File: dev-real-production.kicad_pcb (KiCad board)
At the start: 4 copper layers, 105 x 105 mm, 320 parts, among them IC1 ICM-42670-P, IC2 ENS161-BLGT_LGA9_T&R_1k5, J1 VIN_IN, J10 USB-C USB2 DEBUG, J11 ARM_JTAG_10, J12 SOP0_SELECT, J13 SOP1_SELECT, J14 Conn_01x03, J15 Conn_01x03, J16 ARM_JTAG_10, J17 USB-C Receptacle USB2, J18 Conn_01x03_Pin, J19 Cortex SWD/JTAG, J2 TP_EN_PG, J20 USB-C USB2 DEVICE, J21 HR911105A MAGJACK, J22 Conn_02x10_Counter_Clockwise, J23 Conn_02x04_Odd_Even, J3 TP_SW_FB, J4 USB-C Receptacle USB2, J5 Conn_01x03_Pin, J6 ARM_Cortex_Debug_10, J7 SMA_ANT_50OHM, J8 3V3_IN, U1 MMC5633NJL, U10 USBLC6-2P6, U11 FT230XS-R, U12 FT230XS-R, U13 IWRL6432BDBAAMFR, U14 MX25R1635FZUIH0, U15 MX25R1635FZUIH0, U16 AMS1117-1.8, U17 THS8136, U18 MM8108-MF15457, U19 AP2112K-1.8, U2 LPS22HH, U20 PGA113AIDGSR, U21 AD9609BCPZRL7-80, U22 MCP6D11T-E/MS, U23 STM32H7S3Z8T6, U24 LAN8742A-CZ-TR, U25 USBLC6-2SC6, U3 MIC28516T-E/PHA, U4 RP2350B, U5 XCC1352R1F3RGZR, U6 XMSSJJ3G0PA-054, U7 TLV75518PDBV, U8 TLV75518PDBVR, U9 USBLC6-2P6, Y1 12MHz ABM8-272-T3, Y2 48MHz, Y3 40MHz, Y4 40MHz, Y5 24MHz, Y6 32.768kHz, Y7 25MHz

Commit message: pcb: clean basic DRC findings and document remaining work
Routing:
- net /XCC1352R1F3RGZR/DIO_20: track 135.2 -> 100.4 mm, vias 5 -> 4
- net /XCC1352R1F3RGZR/DIO_26: track 168.3 -> 136.7 mm
- net /STM32H7/PM0: track 102.9 -> 79.9 mm
- net /THX8136/M2: track 176.6 -> 159.4 mm
- net /XCC1352R1F3RGZR/DIO_11: track 138.8 -> 123.2 mm
- net /IWRL6432BD/JTAG_TCK: track 61.8 -> 46.3 mm
- net /RP2350/GPIO7: track 117.0 -> 101.7 mm
- net /STM32H7/PM2: track 85.8 -> 73.0 mm
- net /STM32H7/PM3: track 121.8 -> 114.3 mm
- net /XCC1352R1F3RGZR/DIO_19: track 110.3 -> 103.4 mm
- net /AD9609/RBIAS: track 59.7 -> 53.7 mm
- net /XCC1352R1F3RGZR/DIO_21: track 124.9 -> 119.4 mm
- net /STM32H7/PHY_TXN: track 51.2 -> 45.9 mm
- net /IWRL6432BD/FT_TXD: track 38.1 -> 34.4 mm, vias 6 -> 5
- net /STM32H7/PB5: track 76.0 -> 72.3 mm
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
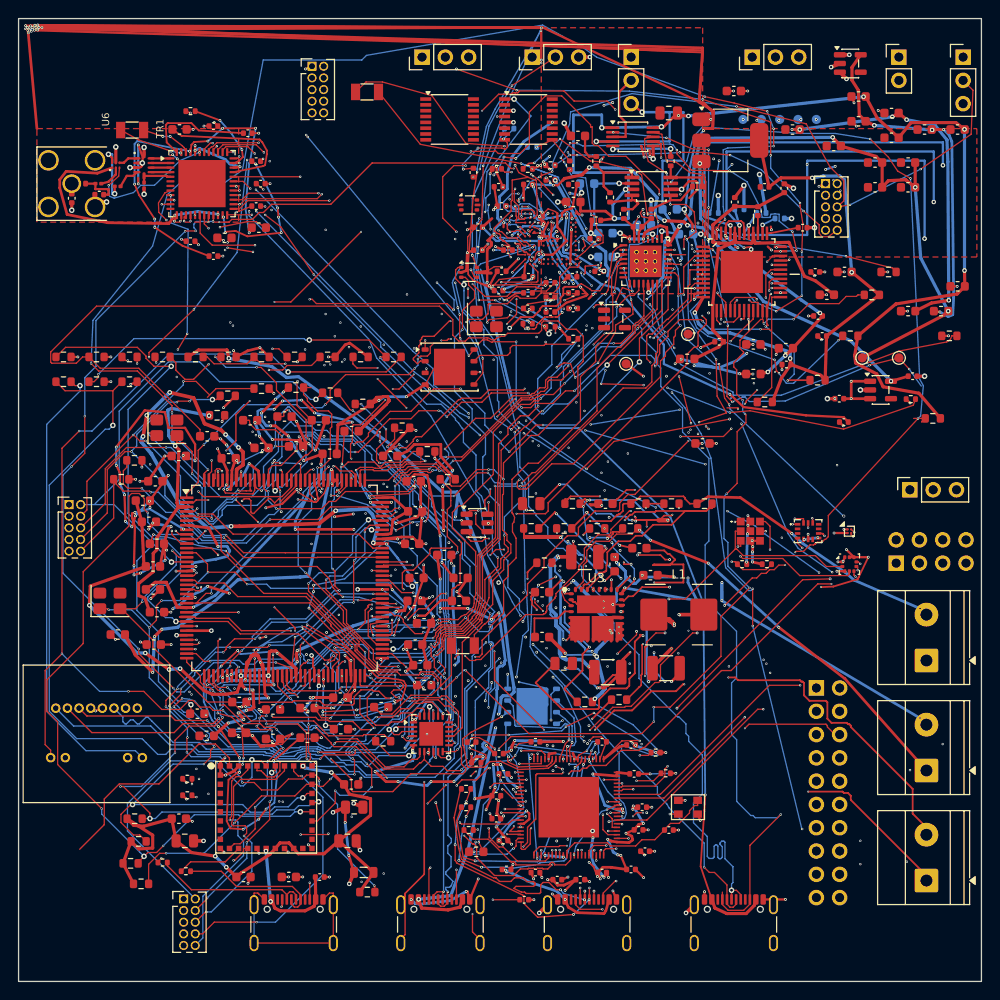
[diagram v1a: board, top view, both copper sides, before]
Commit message: pcb: remove dangling copper and refill zones
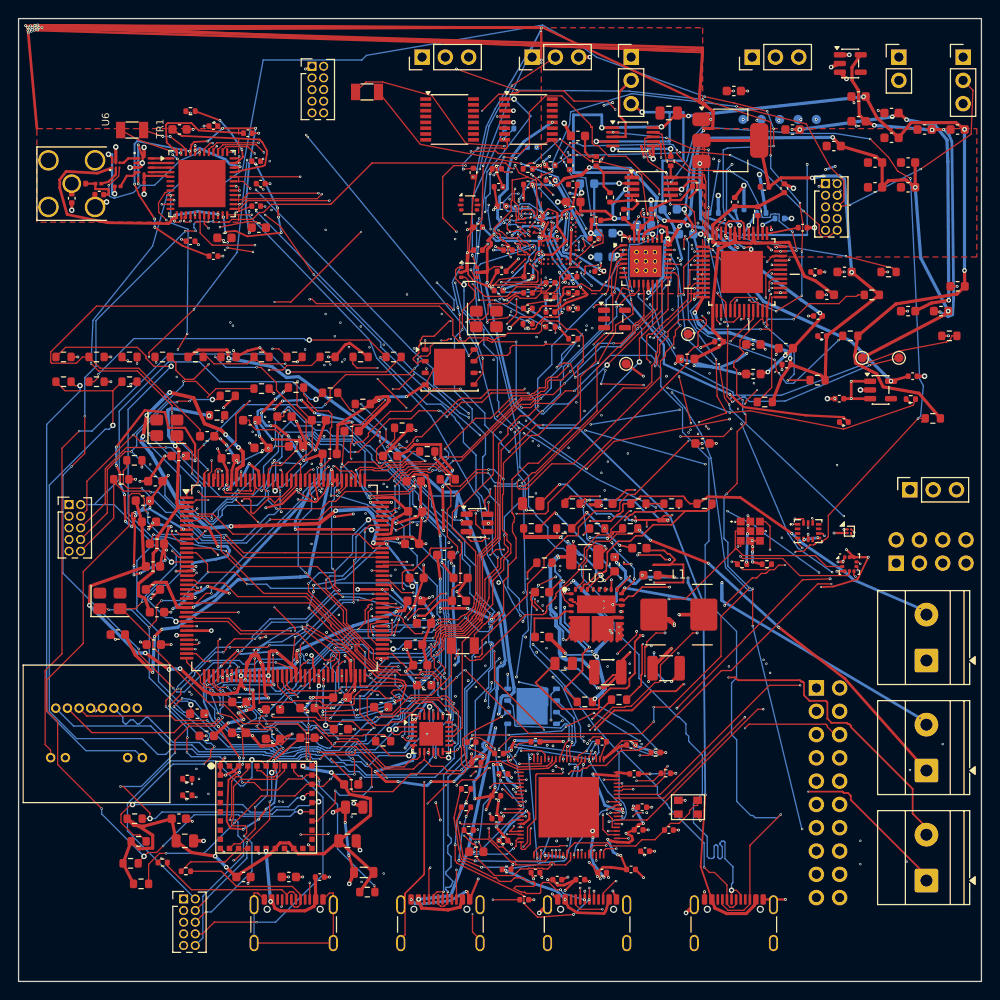
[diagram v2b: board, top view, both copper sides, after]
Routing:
- net /THX8136/AB: track 60.3 -> 23.7 mm, vias 4 -> 3
- net /THX8136/AR: track 51.9 -> 17.3 mm, vias 4 -> 3
- net /THX8136/AG: track 53.1 -> 23.7 mm, vias 4 -> 3
- net /STM32H7/RJ_LED_GREEN_A: track 101.9 -> 77.5 mm, vias 5 -> 2
- net /MM8108/ANT: track 24.2 -> 0.00 mm
- net /IWRL6432BD/GPIO_7: track 109.4 -> 90.5 mm
- net /IWRL6432BD/USB_VBUS: track 136.0 -> 119.8 mm
- net +3V3: track 506.9 -> 496.7 mm
- net /STM32H7/PM5: track 93.7 -> 85.4 mm
- net /IWRL6432BD/RADAR_1V4_SYNTH: track 15.6 -> 10.3 mm
- net Net-(U20-CH1): track 62.5 -> 58.5 mm, vias 9 -> 8
- net GND: track 1681.0 -> 1677.8 mm, vias 380 -> 373
- net /IWRL6432BD/RADAR_VBGAP: track 44.2 -> 42.0 mm, vias 3 -> 2
- net /AD9609/DCO: track 158.4 -> 156.5 mm, vias 6 -> 5
- net /AD9609/D9: track 77.2 -> 75.4 mm, vias 10 -> 9
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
